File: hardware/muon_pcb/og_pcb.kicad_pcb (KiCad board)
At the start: 4 copper layers, 65.4 x 67.7 mm, 69 parts, among them J1 Conn_Coaxial, J12 USB_B_Micro, J2 Conn_Coaxial, J4 Micro_SD_Card_Det1, J5 Conn_01x02_Pin, J6 Conn_Coaxial, SW4 SW_Push_Shielded, SW5 SW_Push_Shielded, U1 CD-PA1616D, U12 RP2040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

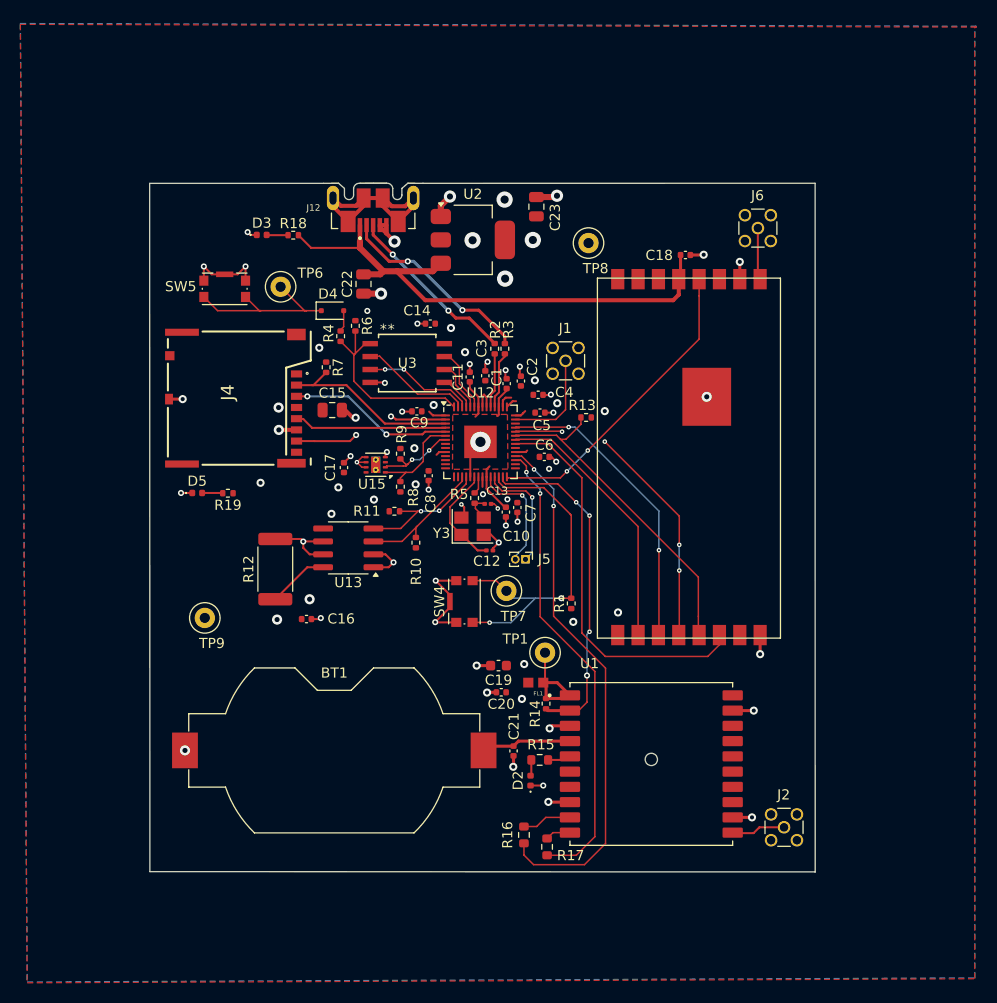
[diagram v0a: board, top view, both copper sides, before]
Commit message: uploaded pcb layout using proves edge cuts
-proves edge cuts with mounting holes
-added credits
-used correct sizes for resistors (based on components picked for resistors)
-to do: pick button, put in df11 connector to supply 5V, determine led being used and resistor values, make sure led wont explode
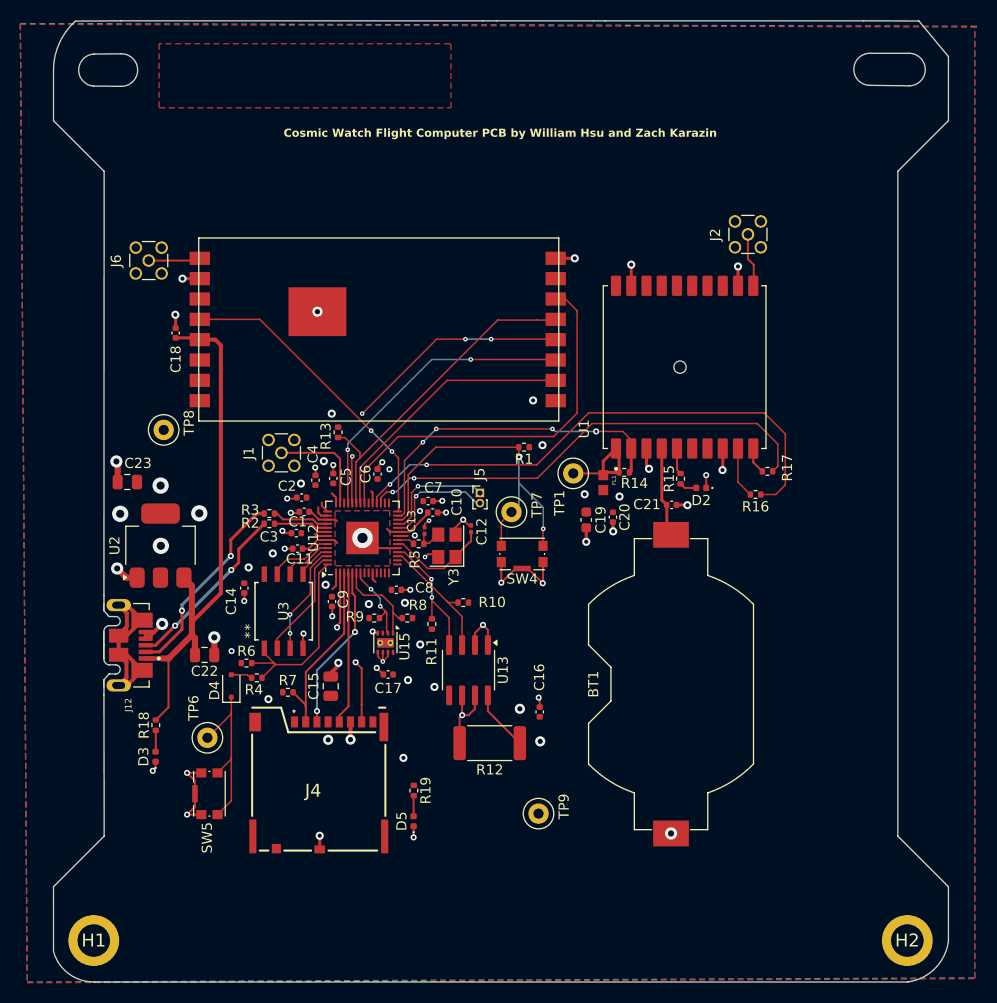
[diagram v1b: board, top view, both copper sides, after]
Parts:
- added G***: LOGO, LOGO, F.Cu at (115.6, 76.8)
- added H1: MountingHole, , F.Cu at (95.2, 161.9)
- added H2: MountingHole, , F.Cu at (175.2, 161.9)
- R15, R16, R17: footprint Resistor_SMD:R_0603_1608Metric -> Resistor_SMD:R_0402_1005Metric
- moved J6 60.0 mm to (100.6, 95.1), turned to 90 degrees
- moved J2 58.4 mm to (159.5, 92.5), turned to 90 degrees
- moved J12 52.6 mm to (96.2, 132.9), turned to -90 degrees
- moved D3 52.4 mm to (101.3, 143.9), turned to 90 degrees
- moved C18 50.7 mm to (103.2, 102.2), turned to -90 degrees
- moved R18 50.0 mm to (101.3, 140.8), turned to -90 degrees
- moved SW5 49.7 mm to (106.6, 147.5), turned to 90 degrees
- moved C23 48.5 mm to (98.5, 116.8), turned to 180 degrees
- moved TP8 45.6 mm to (102.1, 111.7), turned to 90 degrees
- moved TP6 44.9 mm to (106.4, 142.0), turned to 90 degrees
- moved U2 43.0 mm to (101.8, 123.1), turned to 90 degrees
- moved R17 42.8 mm to (161.4, 115.8), turned to 0 degrees
- moved R16 40.5 mm to (160.3, 118.1), turned to 0 degrees
- moved C22 39.7 mm to (106.1, 133.8), turned to 0 degrees
- moved U1 39.2 mm to (153.3, 105.5), turned to 90 degrees
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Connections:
- J12 pad SH1: GND -> (no net)
- J12 pad SH2: GND -> (no net)
- J12 pad SH3: GND -> (no net)
- J12 pad SH4: GND -> (no net)
- J12 pad SH5: GND -> (no net)
- J12 pad SH6: GND -> (no net)
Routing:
- net Net-(U1-3D-FIX): track 2.29 -> 3.10 mm
- added copper zone on F.Cu, net (none)
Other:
- board size 65.4 x 67.7 mm -> 88 x 94.5 mm
- board text added: "Cosmic Watch Flight Computer PCB by William Hsu and Zach Karazin"

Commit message: updated sma coax connector, moved rf module slightly up, assigned bom for some components
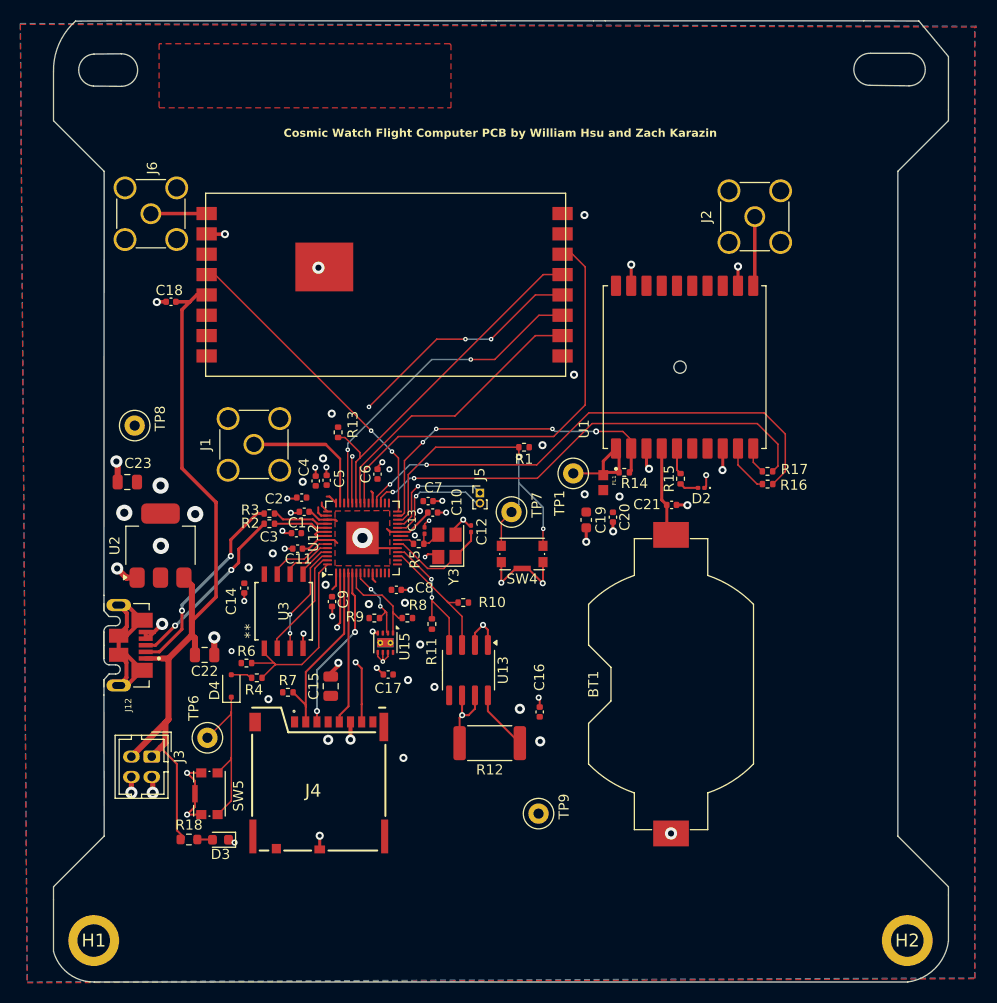
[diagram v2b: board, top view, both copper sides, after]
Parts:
- removed D5: LED, LED_SMD:LED_0402_1005Metric
- removed R19: 10k, Resistor_SMD:R_0402_1005Metric
- added J3: Conn_02x02_Top_Bottom, Connector_Hirose:Hirose_DF11-4DP-2DSA_2x02_P2.00mm_Vertical, F.Cu at (100.9, 143.8)
- D2: footprint LED_SMD:LED_0402_1005Metric -> LED_SMD:LED_0201_0603Metric
- D3: footprint LED_SMD:LED_0402_1005Metric -> LED_SMD:LED_0603_1608Metric
- J1, J2, J6: footprint Connector_Coaxial:MMCX_Molex_73415-1471_Vertical -> Connector_Coaxial:SMA_Amphenol_901-144_Vertical
- R18: footprint Resistor_SMD:R_0402_1005Metric -> Resistor_SMD:R_0603_1608Metric
- moved R18 11.7 mm to (104.6, 152.0), turned to 0 degrees
- moved D3 10.4 mm to (107.7, 152.0), turned to 180 degrees
- moved J6 4.61 mm to (100.8, 90.5)
- moved U16 4.45 mm to (123.9, 98.0)
- moved C18 3.10 mm to (102.8, 99.1), turned to 0 degrees
- moved TP8 2.88 mm to (99.2, 111.3)
- moved J1 2.83 mm to (111.0, 113.2)
- moved J2 1.88 mm to (160.2, 90.8)
- moved R16 1.57 mm to (161.5, 117.0)
- moved C5 0.67 mm to (118.1, 116.7)
- moved C4 0.07 mm to (117.0, 116.7)
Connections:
- J12 pad SH1: (no net) -> GND
- J12 pad SH2: (no net) -> GND
- J12 pad SH3: (no net) -> GND
- J12 pad SH4: (no net) -> GND
- J12 pad SH5: (no net) -> GND
- J12 pad SH6: (no net) -> GND
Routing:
- net VBUS: track 53.2 -> 76.0 mm
- net RF Reset: track 39.1 -> 43.9 mm
- net RF SCK: track 31.3 -> 34.7 mm
- net Cosmic Analog: track 10.4 -> 13.4 mm
- net RF MISO: track 26.3 -> 28.9 mm
- net RF MOSI: track 29.8 -> 32.3 mm
- net RF NSS: track 32.8 -> 35.3 mm
- net GPS UART Tx: track 52.6 -> 50.5 mm
- net Net-(D5-A): track 2.04 -> 0.00 mm
- net GND: track 110.6 -> 109.1 mm, vias 49 -> 50
- net Net-(J2-In): track 6.02 -> 7.36 mm
- net RF DIO4: track 30.5 -> 31.6 mm

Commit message: updated pcb layout
fixed SMA connector footprint, assigned bom to all components except resistors and test points. resistors alr decided on, only need to assign
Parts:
- BT1: footprint Battery:BatteryHolder_Keystone_1058_1x2032 -> 1my_footprints:BAT-TH_BAT-HLD-001-THM_1
- J12: footprint 1my_footprints:microUSB -> 1my_footprints:MICRO-USB-SMD_5P-P0.65-H-F_105164-0001
- SW4, SW5: footprint Button_Switch_SMD:SW_Push_1P1T-SH_NO_CK_KMR2xxG -> Button_Switch_SMD:SW_Push_1P1T_NO_CK_KMR2
- moved BT1 4.81 mm to (155.1, 133.1), turned to 0 degrees
- moved J12 2.60 mm to (98.8, 132.9), turned to 0 degrees
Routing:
- net /Sensors/VBACKUP: track 9.83 -> 47.2 mm
- net GND: track 109.1 -> 139.2 mm, vias 50 -> 58
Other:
- outline, holes or cut-outs redrawn
- board text added: "CADENCE CYGNET CORE COMPUTER PCB by William Hsu and Zach Karazin"
- board text removed: "Cosmic Watch Flight Computer PCB by William Hsu and Zach Karazin"

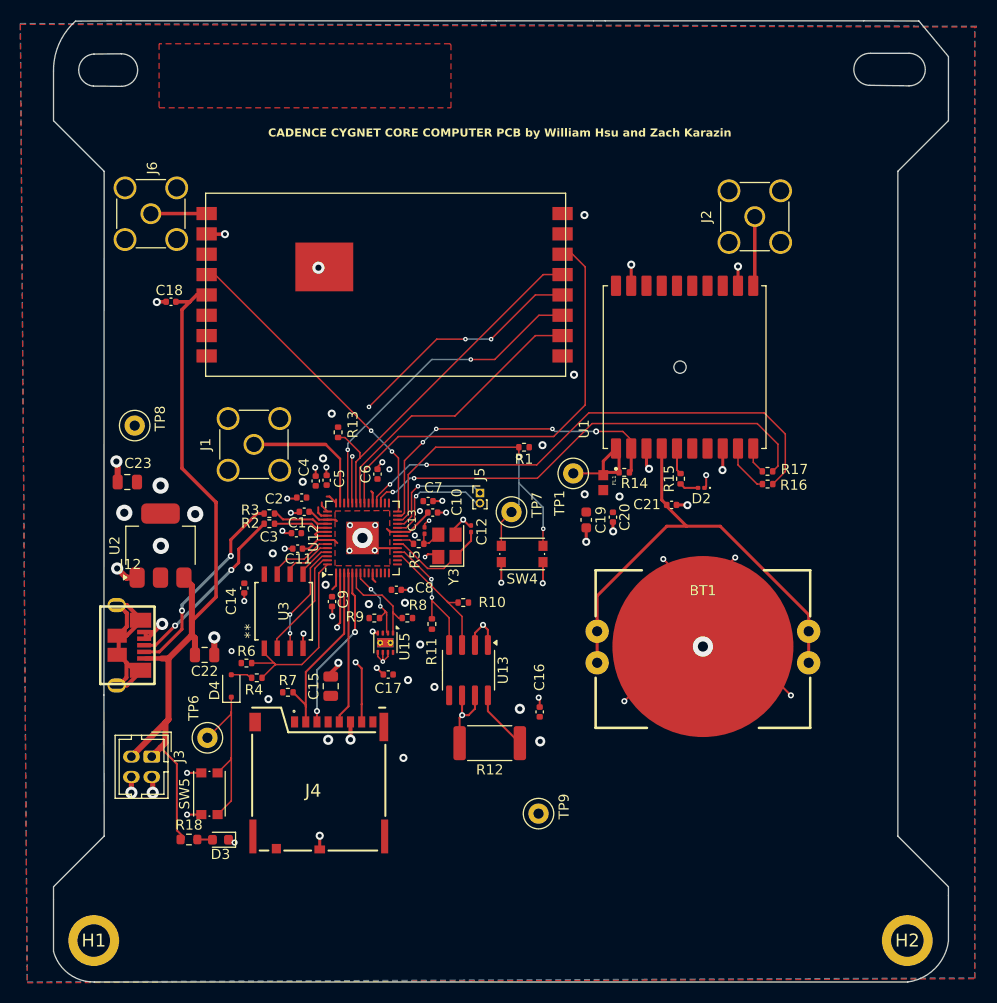
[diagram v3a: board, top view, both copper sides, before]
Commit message: finished assigning bouni tool jlcpcb parts & layout should match components and be good to go
final review
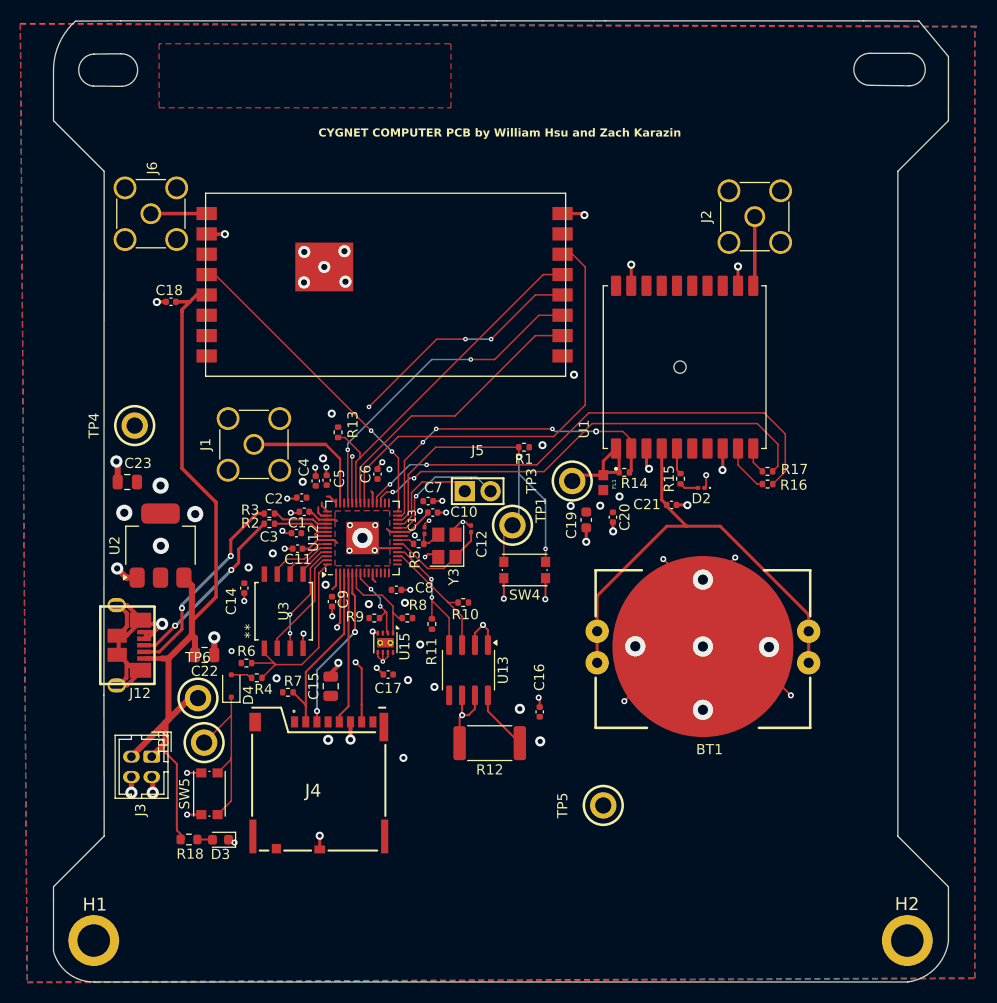
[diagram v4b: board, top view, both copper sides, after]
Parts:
- added TP6: TestPoint, 1my_footprints:TH_BD3.2-D2.0, F.Cu at (105.5, 138.1)
- J5: footprint Connector_PinHeader_1.00mm:PinHeader_1x02_P1.00mm_Vertical -> 1my_footprints:HDR-TH_2P-P2.54-V-M
- TP1: renamed from TP7; footprint 1my_footprints:TestPoint_Loop_D1.80mm_Drill1.0mm_Beaded -> 1my_footprints:TH_BD3.2-D2.0
- TP2: renamed from TP6; footprint 1my_footprints:TestPoint_Loop_D1.80mm_Drill1.0mm_Beaded -> 1my_footprints:TH_BD3.2-D2.0
- TP3: renamed from TP1; footprint 1my_footprints:TestPoint_Loop_D1.80mm_Drill1.0mm_Beaded -> 1my_footprints:TH_BD3.2-D2.0
- TP4: renamed from TP8; footprint 1my_footprints:TestPoint_Loop_D1.80mm_Drill1.0mm_Beaded -> 1my_footprints:TH_BD3.2-D2.0
- TP5: renamed from TP9; footprint 1my_footprints:TestPoint_Loop_D1.80mm_Drill1.0mm_Beaded -> 1my_footprints:TH_BD3.2-D2.0
- moved TP5 6.42 mm to (145.3, 148.7)
- moved SW4 1.59 mm to (137.6, 125.5)
- moved TP1 1.30 mm to (136.4, 121.1)
- moved TP3 0.76 mm to (142.2, 116.8)
- moved TP2 0.58 mm to (106.0, 142.5)
- moved J5 0.29 mm to (132.9, 117.8)
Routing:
- net RP2040 Reset: track 34.8 -> 39.1 mm
- net GND: track 139.2 -> 143.5 mm, vias 58 -> 66
- net VBUS: track 76.0 -> 79.7 mm
- net SWCLK: track 11.3 -> 13.1 mm
- net SWD: track 11.3 -> 10.1 mm, vias 1 -> 0
- net Net-(U1-VCC): track 10.3 -> 10.8 mm
- net +3.3V: vias 28 -> 29
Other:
- board text added: "CYGNET COMPUTER PCB by William Hsu and Zach Karazin"
- board text removed: "CADENCE CYGNET CORE COMPUTER PCB by William Hsu and Zach Karazin"

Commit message: final one maybe
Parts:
- moved SW5 1.00 mm to (107.0, 146.6), turned to 180 degrees
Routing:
- net Net-(D4-K): track 18.1 -> 15.5 mm
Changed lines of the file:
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@@
 		(at 99.225 111.3 90)
 		(property "Reference" "TP4"
-			(at 0 -4 90)
+			(at 0.125 2.85 90)
 			(layer "F.SilkS")
 			(effects
@@
 	(footprint "Button_Switch_SMD:SW_Push_1P1T_NO_CK_KMR2"
 		(layer "F.Cu")
-		(at 106.575 147.5 90)
+		(at 106.95 146.575 180)
 		(descr "CK components KMR2 tactile switch http://www.ckswitches.com/media/1479/kmr2.pdf")
 		(tags "tactile switch kmr2")
 		(property "Reference" "SW5"
-			(at 0 -2.45 90)
+			(at 0 -2.45 0)
 			(layer "F.SilkS")
 			(effects
@@
 		)
 		(property "Value" "SW_Push_Shielded"
-			(at 0 2.55 90)
+			(at 0 2.55 0)
 			(layer "F.Fab")
 			(effects
@@
 		)
 		(property "Datasheet" ""
-			(at 0 0 90)
+			(at 0 0 180)
 			(unlocked yes)
 			(layer "F.Fab")
@@
 		)
 		(property "Description" "Generic push-button switch, two contact pins and shield pin(s)"
-			(at 0 0 90)
+			(at 0 0 180)
 			(unlocked yes)
 			(layer "F.Fab")
@@
 		)
 		(property "LCSC" "C99271"
-			(at 0 0 0)
+			(at 0 0 90)
 			(layer "F.SilkS")
 			(hide yes)
@@
 		(attr smd)
 		(fp_line
-			(start 2.2 -1.55)
-			(end -2.2 -1.55)
+			(start 2.2 0.05)
+			(end 2.2 -0.05)
 			(stroke
 				(width 0.12)
@@
 		)
 		(fp_line
-			(start 2.2 0.05)
-			(end 2.2 -0.05)
+			(start 2.2 -1.55)
+			(end -2.2 -1.55)
 			(stroke
 				(width 0.12)
@@
 		)
 		(fp_line
-			(start -2.2 0.05)
-			(end -2.2 -0.05)
+			(start -2.2 1.55)
+			(end 2.2 1.55)
 			(stroke
 				(width 0.12)
@@
 		)
 		(fp_line
-			(start -2.2 1.55)
-			(end 2.2 1.55)
+			(start -2.2 0.05)
+			(end -2.2 -0.05)
 			(stroke
 				(width 0.12)
@@
 		)
 		(fp_line
-			(start 2.8 -1.8)
-			(end 2.8 1.8)
+			(start 2.8 1.8)
+			(end -2.8 1.8)
 			(stroke
 				(width 0.05)
@@
 		)
 		(fp_line
-			(start -2.8 -1.8)
-			(end 2.8 -1.8)
+			(start 2.8 -1.8)
+			(end 2.8 1.8)
 			(stroke
 				(width 0.05)
@@
 		)
 		(fp_line
-			(start 2.8 1.8)
-			(end -2.8 1.8)
+			(start -2.8 1.8)
+			(end -2.8 -1.8)
 			(stroke
 				(width 0.05)
@@
 		)
 		(fp_line
-			(start -2.8 1.8)
-			(end -2.8 -1.8)
+			(start -2.8 -1.8)
+			(end 2.8 -1.8)
 			(stroke
 				(width 0.05)
@@
 		)
 		(fp_line
-			(start 2.1 -1.4)
-			(end 2.1 1.4)
+			(start 2.1 1.4)
+			(end -2.1 1.4)
 			(stroke
 				(width 0.1)
@@
 		)
 		(fp_line
-			(start -2.1 -1.4)
-			(end 2.1 -1.4)
+			(start 2.1 -1.4)
+			(end 2.1 1.4)
 			(stroke
 				(width 0.1)
@@
 		)
 		(fp_line
-			(start 2.1 1.4)
-			(end -2.1 1.4)
+			(start -2.1 1.4)
+			(end -2.1 -1.4)
 			(stroke
 				(width 0.1)
@@
 		)
 		(fp_line
-			(start -2.1 1.4)
-			(end -2.1 -1.4)
+			(start -2.1 -1.4)
+			(end 2.1 -1.4)
 			(stroke
 				(width 0.1)
@@
 		)
 		(fp_text user "${REFERENCE}"
-			(at 0 -2.45 90)
+			(at 0 -2.45 0)
 			(layer "F.Fab")
 			(effects
@@
 		)
 		(pad "1" smd rect
-			(at -2.05 -0.8 90)
+			(at -2.05 -0.8 180)
 			(size 0.9 1)
 			(layers "F.Cu" "F.Mask" "F.Paste")
@@
 		)
 		(pad "1" smd rect
-			(at 2.05 -0.8 90)
+			(at 2.05 -0.8 180)
 			(size 0.9 1)
 			(layers "F.Cu" "F.Mask" "F.Paste")
@@
 		)
 		(pad "2" smd rect
-			(at -2.05 0.8 90)
+			(at -2.05 0.8 180)
 			(size 0.9 1)
 			(layers "F.Cu" "F.Mask" "F.Paste")
@@
 		)
 		(pad "2" smd rect
-			(at 2.05 0.8 90)
+			(at 2.05 0.8 180)
 			(size 0.9 1)
 			(layers "F.Cu" "F.Mask" "F.Paste")
@@
 		(at 106.05 142.475 90)
 		(property "Reference" "TP2"
-			(at 0 -4 90)
+			(at 0.075 2.925 90)
 			(layer "F.SilkS")
 			(effects
@@
 	)
 	(segment
+		(start 104.725 148.675)
+		(end 104.725 147.55)
+		(width 0.2)
+		(layer "F.Cu")
+		(net 5)
+	)
+	(segment
 		(start 131.415 137.825)
 		(end 131.415 139.765)
@@
 	)
 	(segment
+		(start 109.075 147.45)
+		(end 109 147.375)
+		(width 0.2)
+		(layer "F.Cu")
+		(net 5)
+	)
+	(segment
 		(start 117.025 116.195)
 		(end 117.025 115.475)
@@
 	)
 	(segment
+		(start 104.725 147.55)
+		(end 104.9 147.375)
+		(width 0.2)
+		(layer "F.Cu")
+		(net 5)
+	)
+	(segment
 		(start 152.75 133.025)
 		(end 147.375 138.4)
@@
 	)
 	(segment
+		(start 109.075 148.7)
+		(end 109.075 147.45)
+		(width 0.2)
+		(layer "F.Cu")
+		(net 5)
+	)
+	(segment
 		(start 149.55 113.55)
 		(end 149.55 115.3)
@@
 	)
 	(segment
-		(start 105.775 149.55)
-		(end 104.375 149.55)
-		(width 0.2)
-		(layer "F.Cu")
-		(net 5)
-	)
-	(segment
 		(start 155.1 133.025)
 		(end 158.95 133.025)
@@
 	)
 	(segment
-		(start 105.775 145.45)
-		(end 104.375 145.45)
-		(width 0.2)
-		(layer "F.Cu")
-		(net 5)
-	)
-	(segment
 		(start 99.8 135.36)
 		(end 99.8 135.5125)
@@
 	)
 	(via
-		(at 104.375 149.55)
+		(at 104.725 148.675)
 		(size 0.6)
 		(drill 0.3)
@@
 	)
 	(via
-		(at 104.375 145.45)
+		(at 109.075 148.7)
 		(size 0.6)
 		(drill 0.3)
@@
 		(start 118 113.15)
 		(end 110.95 113.15)
-		(width 0.35)
+		(width 0.15)
 		(layer "F.Cu")
 		(net 9)
@@
 		(start 119.425 118.9125)
 		(end 119.425 114.575)
-		(width 0.2)
+		(width 0.15)
 		(layer "F.Cu")
 		(net 9)
@@
 		(start 119.425 114.575)
 		(end 118 113.15)
-		(width 0.25)
+		(width 0.15)
 		(layer "F.Cu")
 		(net 9)
@@
 	)
 	(segment
-		(start 108.725 139.8)
-		(end 108.725 144.025)
-		(width 0.15)
-		(layer "F.Cu")
-		(net 67)
-	)
-	(segment
-		(start 108.725 143.95)
-		(end 108.725 144.025)
+		(start 108.65 138)
+		(end 108.725 138)
 		(width 0.15)
 		(layer "F.Cu")
@@
 	)
 	(segment
-		(start 108.725 144.025)
-		(end 108.725 144.1)
+		(start 104.9 143.625)
+		(end 106.05 142.475)
 		(width 0.15)
 		(layer "F.Cu")
@@
 	)
 	(segment
-		(start 108.65 138)
-		(end 108.725 138)
+		(start 104.9 145.775)
+		(end 104.9 143.625)
 		(width 0.15)
 		(layer "F.Cu")
@@
 	)
 	(segment
-		(start 108.725 144.1)
-		(end 107.375 145.45)
+		(start 109 144.375)
+		(end 109 145.775)
 		(width 0.15)
 		(layer "F.Cu")
@@
 	)
 	(segment
-		(start 108.725 143.95)
-		(end 108.725 148.2)
+		(start 106.05 142.475)
+		(end 108.725 139.8)
 		(width 0.15)
 		(layer "F.Cu")
@@
 	)
 	(segment
-		(start 108.725 148.2)
-		(end 107.375 149.55)
+		(start 108.725 144.1)
+		(end 109 144.375)
 		(width 0.15)
 		(layer "F.Cu")
@@
 	)
 	(segment
-		(start 106.05 142.475)
-		(end 108.725 139.8)
+		(start 108.725 139.8)
+		(end 108.725 144.1)
 		(width 0.15)
 		(layer "F.Cu")
